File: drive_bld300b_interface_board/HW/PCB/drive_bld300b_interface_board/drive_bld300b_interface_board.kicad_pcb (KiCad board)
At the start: 2 copper layers, 101.6 x 86.4 mm, 6 parts, among them J1 N_CN7, J2 M1, J3 N_CN10, J4 M2, J5 M3, J6 M4

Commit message: Finished PCB
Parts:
- added REF**: M3, MountingHole:MountingHole_3.2mm_M3, F.Cu at (161.3, 132.1)
- added REF**: M3, MountingHole:MountingHole_3.2mm_M3, F.Cu at (100.3, 132.1)
- added REF**: M3, MountingHole:MountingHole_3.2mm_M3, F.Cu at (151.1, 83.8)
- added REF**: M3, MountingHole:MountingHole_3.2mm_M3, F.Cu at (110.5, 83.8)
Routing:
- net /M2_SPD: track 159.3 -> 154.2 mm
- net /M2_HC: track 152.2 -> 147.4 mm
- added copper zone on B.Cu, net GND
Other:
- board text added: "FRANCOR e.V. BLDC BLD-300B Interface Board"

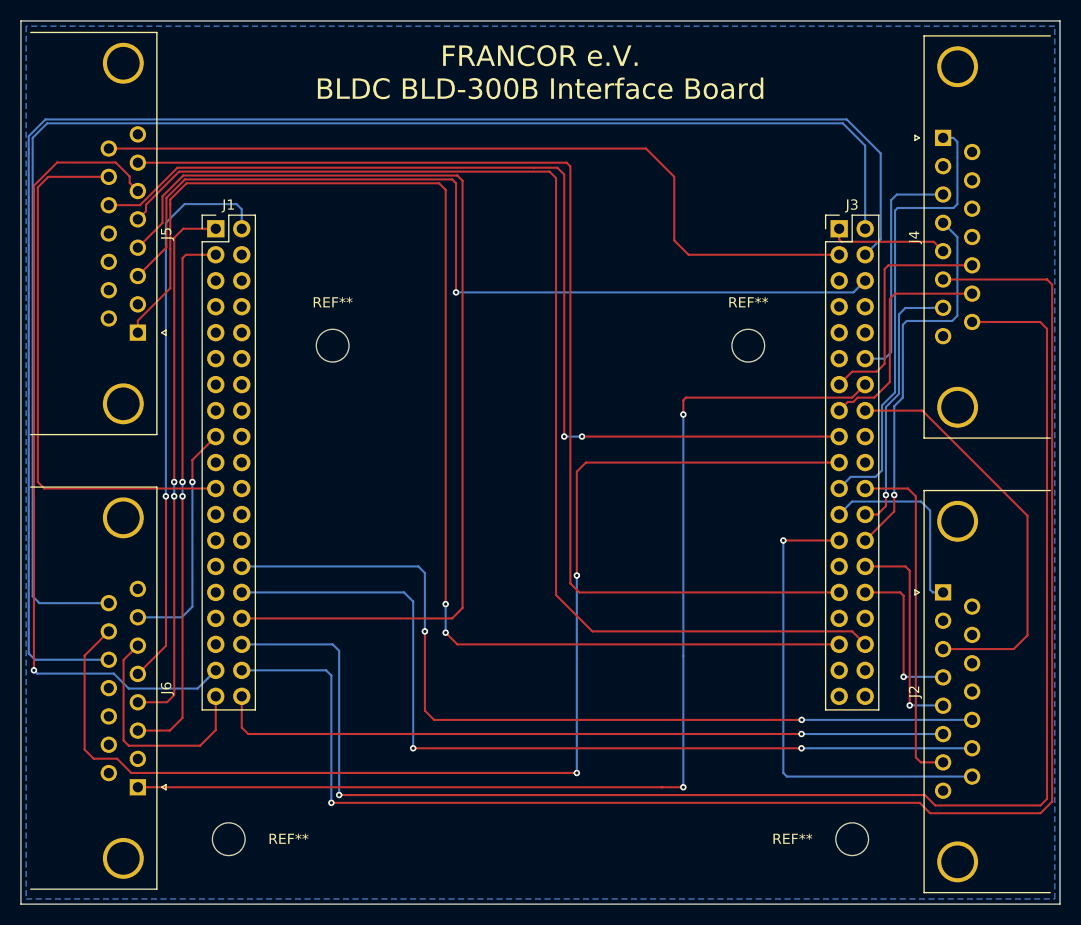
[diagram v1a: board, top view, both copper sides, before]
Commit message: Added text to PCBs
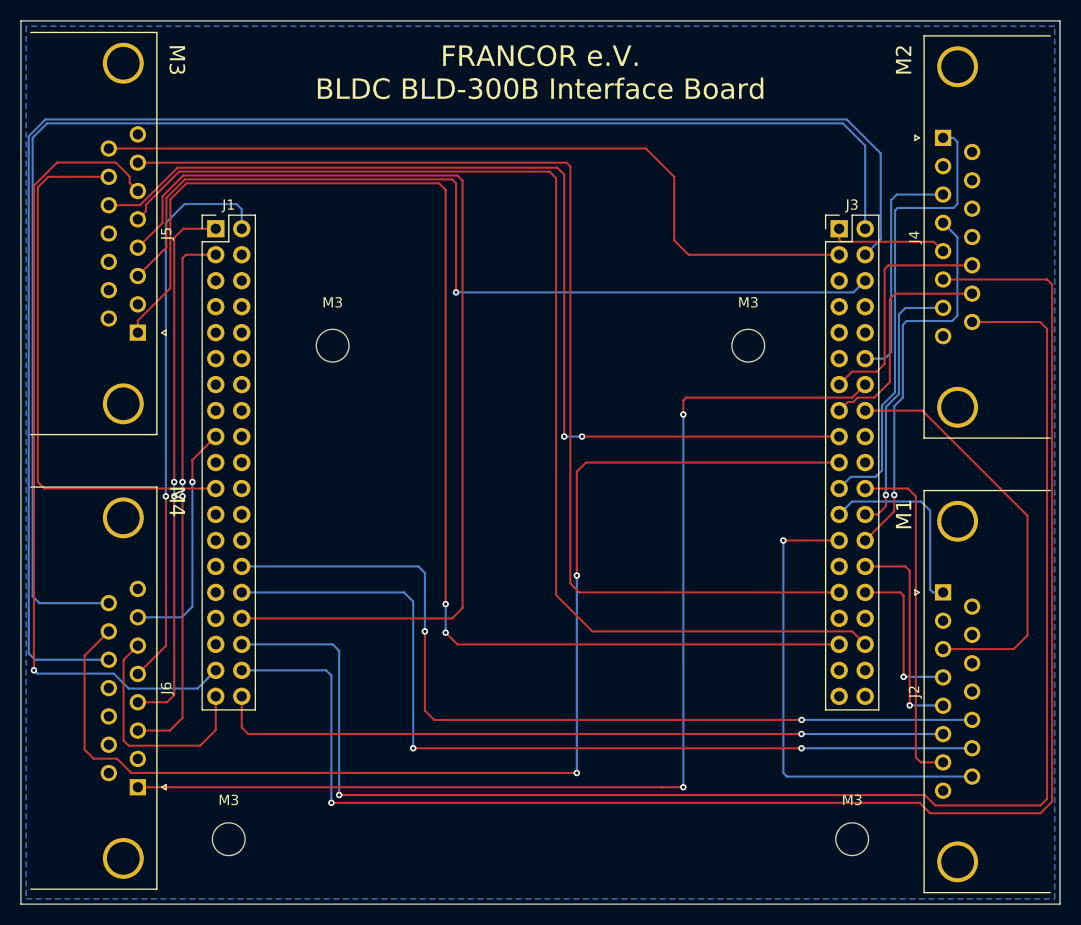
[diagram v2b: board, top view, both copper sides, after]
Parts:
- removed REF** (x3): M3, MountingHole:MountingHole_3.2mm_M3
- added M3: M3, MountingHole:MountingHole_3.2mm_M3, F.Cu at (161.3, 132.1)
- added M3: M3, MountingHole:MountingHole_3.2mm_M3, F.Cu at (100.3, 132.1)
- added M3: M3, MountingHole:MountingHole_3.2mm_M3, F.Cu at (151.1, 83.8)
- renumbered REF** to M3
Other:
- board text added: "M1"
- board text added: "M2"
- board text added: "M3"
- board text added: "M4"
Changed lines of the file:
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@@
   (general
     (thickness 1.6)
-    (drawings 7)
+    (drawings 11)
     (tracks 306)
     (zones 0)
@@
     (tags "mounting hole 3.2mm no annular m3")
     (attr virtual)
-    (fp_text reference REF** (at -5.842 0) (layer F.SilkS)
+    (fp_text reference M3 (at 0 -3.81) (layer F.SilkS)
       (effects (font (size 1 1) (thickness 0.15)))
     )
@@
     (tags "mounting hole 3.2mm no annular m3")
     (attr virtual)
-    (fp_text reference REF** (at 5.842 0) (layer F.SilkS)
+    (fp_text reference M3 (at 0 -3.81) (layer F.SilkS)
       (effects (font (size 1 1) (thickness 0.15)))
     )
@@
     (tags "mounting hole 3.2mm no annular m3")
     (attr virtual)
-    (fp_text reference REF** (at 0 -4.2) (layer F.SilkS)
+    (fp_text reference M3 (at 0 -4.2) (layer F.SilkS)
       (effects (font (size 1 1) (thickness 0.15)))
     )
@@
     (tags "mounting hole 3.2mm no annular m3")
     (attr virtual)
-    (fp_text reference REF** (at 0 -4.2) (layer F.SilkS)
+    (fp_text reference M3 (at 0 -4.2) (layer F.SilkS)
       (effects (font (size 1 1) (thickness 0.15)))
     )
@@
     )
   )
+  (gr_text M4 (at 95.25 99.06 270) (layer F.SilkS)
+    (effects (font (size 1.5 1.5) (thickness 0.3)))
+  )
+  (gr_text M3 (at 95.25 55.88 270) (layer F.SilkS)
+    (effects (font (size 1.5 1.5) (thickness 0.3)))
+  )
+  (gr_text M2 (at 166.37 55.88 90) (layer F.SilkS)
+    (effects (font (size 1.5 1.5) (thickness 0.3)))
+  )
+  (gr_text M1 (at 166.37 100.33 90) (layer F.SilkS)
+    (effects (font (size 1.5 1.5) (thickness 0.3)))
+  )
   (dimension 86.36 (width 0.15) (layer Dwgs.User)
